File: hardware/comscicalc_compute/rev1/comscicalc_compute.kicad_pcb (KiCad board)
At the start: 4 copper layers, 94 x 29 mm, 76 parts, among them IC2 TPS92360DCKR, IC4 FT811Q-T, J1 TSM-110-01-L-DV-A-P-TR, J2 TSM-110-01-L-DV-A-P-TR, J3 USB4110-GF-A, J4 4-1734839-0, SW1 JS202011JAQN, SW2 JS202011JAQN, U1 USBLC6-2SC6, U2 W25Q32JVSSIQ, U3 RP2040, U4 TPSM863253, Y1 445I23D12M00000, Y2 ECS-2520MV-120-BN-TR

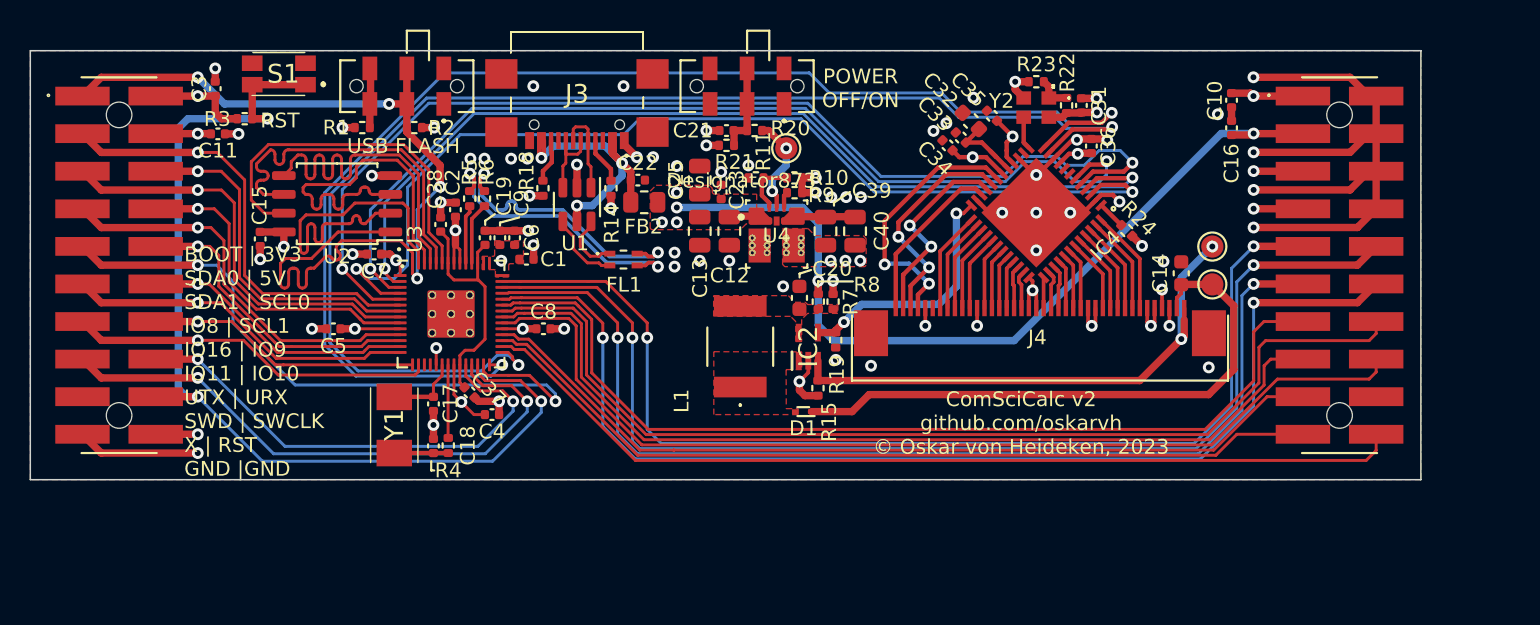
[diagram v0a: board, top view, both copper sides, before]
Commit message: Added hardware changes and some of the missing fonts
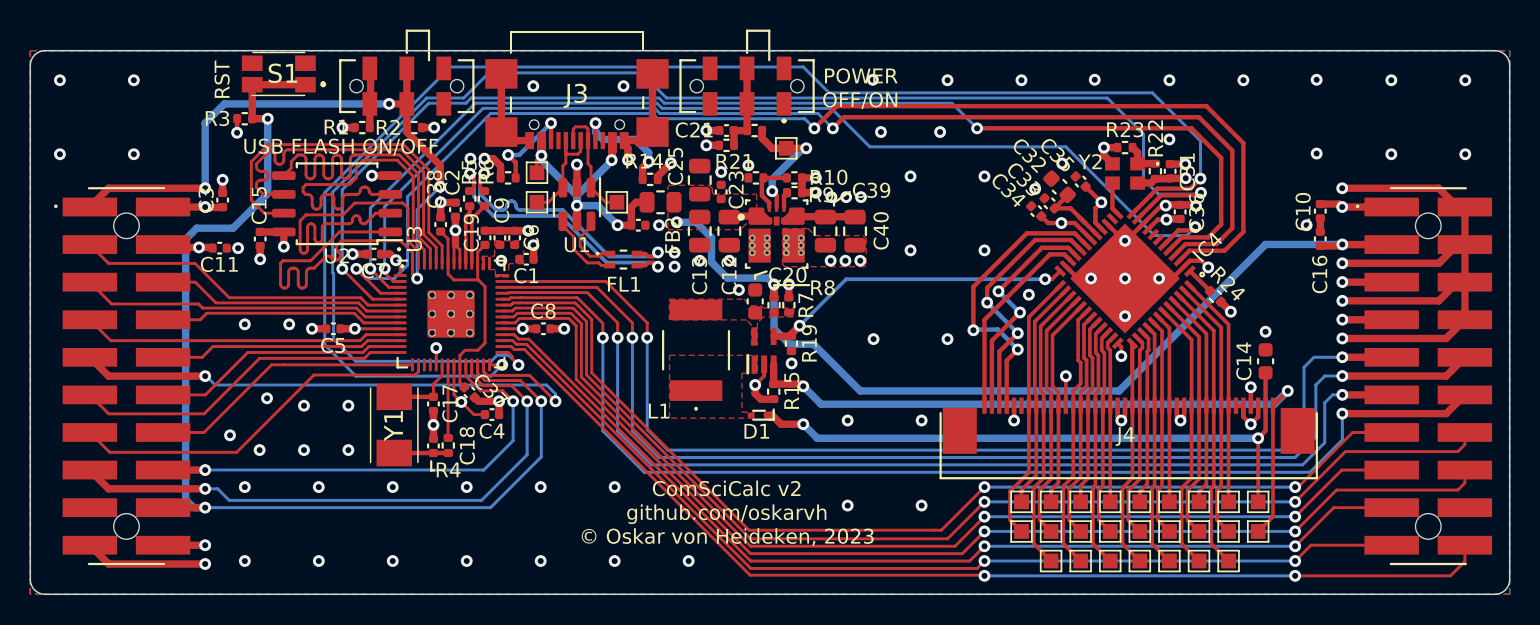
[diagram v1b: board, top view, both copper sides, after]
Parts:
- removed TP4, TP5: TestPoint, TestPoint:TestPoint_Pad_D1.5mm
- added TB_PCLK1: TestPoint_Small, TestPoint:TestPoint_Pad_1.0x1.0mm, F.Cu at (114.5, 93.5)
- added TPB2: TestPoint_Small, TestPoint:TestPoint_Pad_1.0x1.0mm, F.Cu at (118.5, 93.5)
- added TPB3: TestPoint_Small, TestPoint:TestPoint_Pad_1.0x1.0mm, F.Cu at (118.5, 95.5)
- added TPB4: TestPoint_Small, TestPoint:TestPoint_Pad_1.0x1.0mm, F.Cu at (118.5, 97.5)
- added TPB5: TestPoint_Small, TestPoint:TestPoint_Pad_1.0x1.0mm, F.Cu at (116.5, 93.5)
- added TPB6: TestPoint_Small, TestPoint:TestPoint_Pad_1.0x1.0mm, F.Cu at (116.5, 95.5)
- added TPB7: TestPoint_Small, TestPoint:TestPoint_Pad_1.0x1.0mm, F.Cu at (116.5, 97.5)
- added TPDR1: TestPoint_Small, TestPoint:TestPoint_Pad_1.0x1.0mm, F.Cu at (128.5, 93.5)
- added TPDR2: TestPoint_Small, TestPoint:TestPoint_Pad_1.0x1.0mm, F.Cu at (128.5, 95.5)
- added TPDR3: TestPoint_Small, TestPoint:TestPoint_Pad_1.0x1.0mm, F.Cu at (79.8, 71.2)
- added TPG2: TestPoint_Small, TestPoint:TestPoint_Pad_1.0x1.0mm, F.Cu at (122.5, 93.5)
- added TPG3: TestPoint_Small, TestPoint:TestPoint_Pad_1.0x1.0mm, F.Cu at (122.5, 95.5)
- added TPG4: TestPoint_Small, TestPoint:TestPoint_Pad_1.0x1.0mm, F.Cu at (122.5, 97.5)
- added TPG5: TestPoint_Small, TestPoint:TestPoint_Pad_1.0x1.0mm, F.Cu at (120.5, 93.5)
- added TPG6: TestPoint_Small, TestPoint:TestPoint_Pad_1.0x1.0mm, F.Cu at (120.5, 95.5)
- added TPG7: TestPoint_Small, TestPoint:TestPoint_Pad_1.0x1.0mm, F.Cu at (120.5, 97.5)
- added TPR1: TestPoint_Small, TestPoint:TestPoint_Pad_1.0x1.0mm, F.Cu at (79.8, 73.2)
- added TPR2: TestPoint_Small, TestPoint:TestPoint_Pad_1.0x1.0mm, F.Cu at (126.5, 93.5)
- added TPR3: TestPoint_Small, TestPoint:TestPoint_Pad_1.0x1.0mm, F.Cu at (126.5, 95.5)
- added TPR4: TestPoint_Small, TestPoint:TestPoint_Pad_1.0x1.0mm, F.Cu at (126.5, 97.5)
- added TPR5: TestPoint_Small, TestPoint:TestPoint_Pad_1.0x1.0mm, F.Cu at (124.5, 93.5)
- added TPR6: TestPoint_Small, TestPoint:TestPoint_Pad_1.0x1.0mm, F.Cu at (124.5, 95.5)
- added TPR7: TestPoint_Small, TestPoint:TestPoint_Pad_1.0x1.0mm, F.Cu at (124.5, 97.5)
- added TPR8: TestPoint_Small, TestPoint:TestPoint_Pad_1.0x1.0mm, F.Cu at (85.2, 73.2)
- added TP_DE1: TestPoint_Small, TestPoint:TestPoint_Pad_1.0x1.0mm, F.Cu at (112.5, 95.5)
- added TP_DISP1: TestPoint_Small, TestPoint:TestPoint_Pad_1.0x1.0mm, F.Cu at (114.5, 95.5)
- added TP_HSYNC1: TestPoint_Small, TestPoint:TestPoint_Pad_1.0x1.0mm, F.Cu at (114.5, 97.5)
- added TP_VSYNC1: TestPoint_Small, TestPoint:TestPoint_Pad_1.0x1.0mm, F.Cu at (112.5, 93.5)
- TP1: footprint TestPoint:TestPoint_Pad_D1.5mm -> TestPoint:TestPoint_Pad_1.0x1.0mm
- moved J2 9.60 mm to (140.0, 85.0)
- moved C10 9.60 mm to (132.7, 73.8)
- moved C16 9.60 mm to (132.7, 75.7)
- moved J4 8.92 mm to (119.8, 91.9)
- moved C14 8.24 mm to (129.0, 84.0)
- moved C11 7.73 mm to (58.3, 76.3)
- moved C3 7.55 mm to (58.5, 73.1)
- moved J1 7.52 mm to (52.0, 85.0)
- moved C31 7.47 mm to (122.5, 71.2)
- moved C32 7.47 mm to (115.1, 72.2)
- moved C36 7.47 mm to (123.2, 73.9)
- moved IC4 7.47 mm to (119.5, 78.4)
- moved R22 7.47 mm to (121.5, 71.2)
- moved R23 7.47 mm to (119.5, 69.5)
- moved R24 7.47 mm to (125.6, 79.6)
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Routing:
- net /LCD/G7: track 2.07 -> 17.5 mm
- net SPI0_SCK: track 69.3 -> 84.4 mm
- net +5V: track 104.0 -> 117.6 mm, vias 8 -> 5
- net /LCD/HSYNC: track 6.00 -> 19.6 mm
- net /LCD/B7: track 4.55 -> 18.1 mm
- net /LCD/R7: track 4.97 -> 18.4 mm
- net /LCD/B4: track 3.31 -> 16.7 mm
- net /LCD/G4: track 3.31 -> 16.5 mm
- net /LCD/R4: track 6.21 -> 19.4 mm
- net SPI0_MISO: track 64.9 -> 77.5 mm
- net GND: track 126.3 -> 138.3 mm, vias 71 -> 116
- net /LCD/DISP: track 5.59 -> 17.1 mm
- net /LCD/DE: track 6.83 -> 18.3 mm
- net /LCD/B6: track 4.14 -> 15.6 mm
- net /LCD/G6: track 2.63 -> 13.9 mm
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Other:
- board size 94 x 29 mm -> 100 x 36.8 mm
- board text added: "USB FLASH ON/OFF"
- board text removed: "BOOT | 3V3 SDA0 | 5V SDA1 | SCL0 IO8 | SCL1 IO16 | IO9 IO11 | IO10 UTX | URX SWD | SWCLK X | RST GND |GND"
- board text removed: "USB FLASH"

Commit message: Board according to this rev (v2) has been ordered from oshpark.
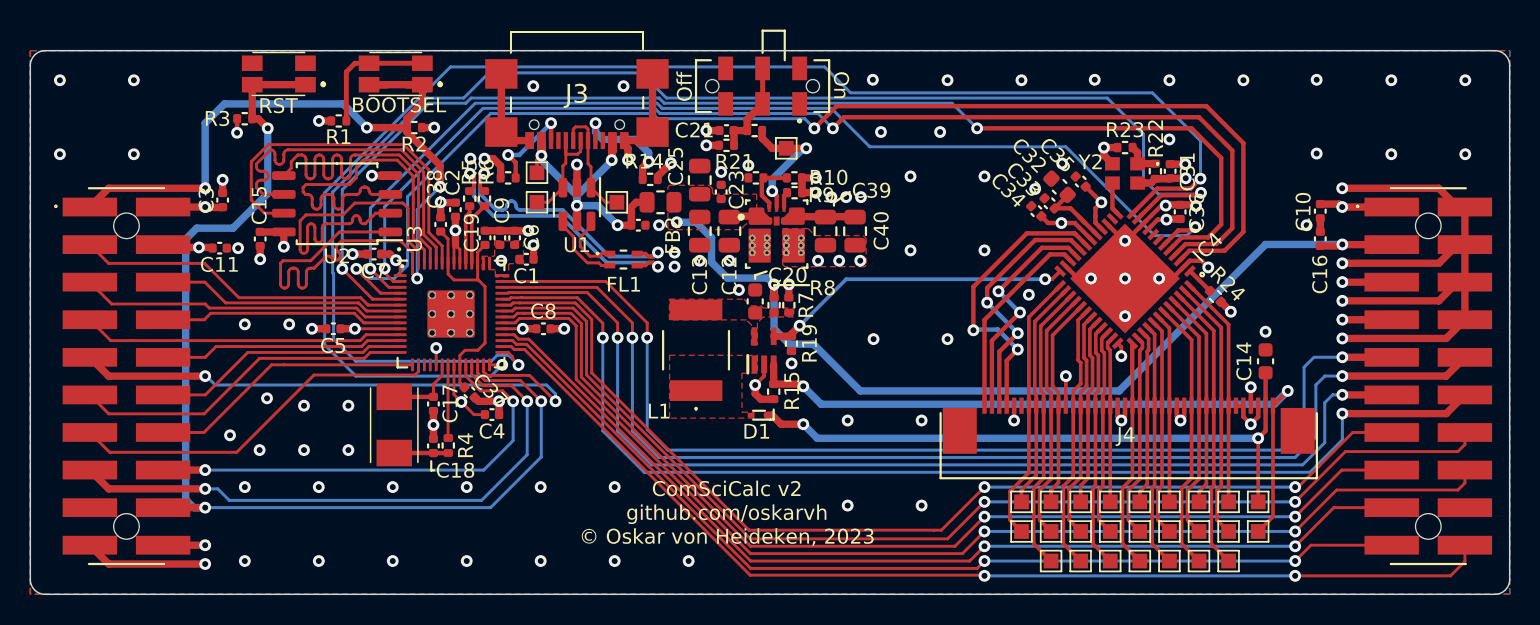
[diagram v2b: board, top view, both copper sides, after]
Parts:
- removed SW1: JS202011JAQN, JS202011JAQN:JS202011JAQN
- added S2: EVQ-P7J01P, SamacSys_Parts:EVQP7J01P, F.Cu at (70.5, 64.6)
- moved R1 1.65 mm to (66.3, 67.8)
- moved SW2 1.05 mm to (95.0, 65.4)
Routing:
- net /MCU/QSPI_CSn: track 68.6 -> 74.5 mm
- net Net-(R1-Pad1): track 4.04 -> 8.69 mm
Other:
- board text added: "BOOTSEL"
- board text added: "Off"
- board text added: "On"
- board text removed: "POWER OFF/ON"
- board text removed: "USB FLASH ON/OFF"
